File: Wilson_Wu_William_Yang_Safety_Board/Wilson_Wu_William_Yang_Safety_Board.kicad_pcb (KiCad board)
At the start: 2 copper layers, 122.4 x 171.4 mm, 115 parts, among them J1 22035035, J18 XT60-M, J2 22035035, J3 430450200, J4 M22-7130442, J5 430450200, J6 XT60-M, J7 XT60-M, J8 430450200, J9 Molex Micro-Fit 4 Pin, Q1 IRLML6344TRPBF, Q2 IRLML6344TRPBF, Q3 NTBLS0D8N08XTXG, Q4 NTBLS0D8N08XTXG, U1 STM32, U10 LTC4364HS, U11 LMV331IDBVR, U12 J115F11AH12VDCS61.5U, U13 ISOM8110DFGRQ1, U15 INA826AID, U16 J115F11AH12VDCS61.5U, U2 MCP2562-E_P, U3 10kohm, U4 SN74HCS21QPWRQ1, U5 J115F11AH12VDCS61.5U, U6 J115F11AH12VDCS61.5U, U7 LM1117IDTX-5.0/NOPB, U8 LM1117IMPX-ADJ/NOPB, U9 100 ohm

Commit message: layout
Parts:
- moved R106 12.0 mm to (95.2, 31.5)
- moved Q4 7.01 mm to (98.2, 38.7)
- moved C17 5.17 mm to (100.6, 21.1)
- moved U10 5.17 mm to (102.2, 25.8)
- moved C104 3.00 mm to (90.0, 32.4)
- moved R107 3.00 mm to (90.0, 30.8)
- moved R108 3.00 mm to (86.9, 30.8)
- moved R109 3.00 mm to (86.9, 32.4)
- moved Q3 0.35 mm to (103.7, 50.3)
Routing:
- net Net-(U10-DGATE): track 0.07 -> 18.8 mm
- net Net-(U10-~{SHDN}): track 11.8 -> 18.0 mm
- net Net-(U10-UV): track 20.9 -> 26.2 mm
- net Net-(D4-K): track 20.3 -> 25.7 mm
- net Net-(U10-OV): track 29.4 -> 34.7 mm

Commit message: holy
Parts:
- moved TP27 17.6 mm to (127.7, 16.6)
- moved C12 17.6 mm to (137.9, 17.5)
- moved J8 17.6 mm to (132.7, 16.6)
- moved TP10 6.66 mm to (103.5, 95.5)
- moved C1 4.78 mm to (132.2, 42.1)
- moved C2 4.78 mm to (140.9, 34.3)
- moved TP17 4.78 mm to (144.1, 34.3)
- moved U7 4.78 mm to (139.7, 38.9)
- moved H1 1.70 mm to (30.0, 163.8)
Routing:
- net Hydrogen-Output: track 116.8 -> 60.2 mm, vias 4 -> 2
- net load switch conn: track 4.82 -> 55.2 mm, vias 0 -> 2
- net Net-(U10-FB): track 1.77 -> 30.8 mm
- net +12V: track 249.9 -> 265.1 mm
- net /PA3: track 32.4 -> 35.5 mm
- net ignition signal: track 54.1 -> 52.0 mm
- net +5V: track 219.9 -> 217.9 mm
- net GND: track 54.1 -> 55.4 mm
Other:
- board size 122.4 x 171.4 mm -> 122.4 x 168.1 mm

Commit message: pcb layout
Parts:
- moved C103 1.19 mm to (108.4, 40.2)
- moved R105 1.19 mm to (108.4, 42.0)
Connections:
- C103 pad 2: Net-(U10-DGATE) -> Net-(U10-HGATE)
- R105 pad 1: Net-(U10-DGATE) -> Net-(U10-HGATE)
- R106 pad 3: (no net) -> load conn
- U10 pad 6: Net-(U10-DGATE) -> Net-(U10-HGATE)
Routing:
- net Net-(U10-HGATE): track 0.00 -> 15.2 mm
- net Net-(U10-DGATE): track 18.8 -> 18.1 mm, vias 0 -> 2
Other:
- board text added: "LTC4364HS"
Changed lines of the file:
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@@
 	(net 126 "Net-(U4-2D)")
 	(net 127 "Net-(U4-2C)")
+	(net 128 "Net-(U10-HGATE)")
 	(footprint "Diode_SMD:D_SOD-523"
 		(layer "F.Cu")
@@
 	(footprint "SMV_Passives:0603_resistors"
 		(layer "F.Cu")
-		(at 107.227799 42.25)
+		(at 108.377799 41.95)
 		(property "Reference" "R105"
 			(at -0.26 -1.1 0)
@@
 			(size 1.04 1.02)
 			(layers "F.Cu" "F.Mask" "F.Paste")
-			(net 39 "Net-(U10-DGATE)")
+			(net 128 "Net-(U10-HGATE)")
 			(pintype "passive")
 			(solder_mask_margin 0.102)
@@
 	(footprint "SMV_Passives:CAPC17595_87N_KEM"
 		(layer "F.Cu")
-		(at 107.25 40.5 180)
+		(at 108.4 40.2 180)
 		(tags "C0603C472K4RACTU ")
 		(property "Reference" "C103"
@@
 			(size 1.005599 0.949998)
 			(layers "F.Cu" "F.Mask" "F.Paste")
-			(net 39 "Net-(U10-DGATE)")
+			(net 128 "Net-(U10-HGATE)")
 			(pintype "passive")
 		)
@@
 			(polygon
 				(pts
-					(xy 107.4242 40.924199) (xy 107.0758 40.924199) (xy 107.0758 40.075801) (xy 107.4242 40.075801)
+					(xy 108.5742 40.624199) (xy 108.2258 40.624199) (xy 108.2258 39.775801) (xy 108.5742 39.775801)
 				)
 			)
@@
 			(layers "F.Cu" "F.Mask" "F.Paste")
 			(roundrect_rratio 0.25)
-			(net 39 "Net-(U10-DGATE)")
+			(net 128 "Net-(U10-HGATE)")
 			(pinfunction "HGATE")
 			(pintype "output")
@@
 			(pintype "passive")
 		)
-		(pad "2" smd rect
+		(pad "3" smd rect
 			(at 2.03 0 180)
 			(size 1.65 1.14)
 			(layers "F.Cu" "F.Mask" "F.Paste")
 			(net 58 "load conn")
-			(pintype "passive")
-		)
-		(pad "3" smd rect
-			(at -1.02 0 180)
-			(size 0.53 1.14)
-			(layers "F.Cu" "F.Mask" "F.Paste")
-		)
-		(pad "4" smd rect
-			(at 1.02 0 180)
-			(size 0.53 1.14)
-			(layers "F.Cu" "F.Mask" "F.Paste")
 		)
 		(embedded_fonts no)
@@
 	(gr_poly
 		(pts
-			(xy 108.5612 45.25) (xy 108.5612 41.8) (xy 107.5 41.8) (xy 107.5 45.25)
-		)
-		(stroke
-			(width 0.2)
-			(type solid)
-		)
-		(fill yes)
-		(layer "F.Cu")
-		(net 77)
-	)
-	(gr_poly
-		(pts
-			(xy 105.765402 39.771001) (xy 106.95 39.771001) (xy 106.95 43) (xy 106.629938 43.362941) (xy 103.35 43.3)
-			(xy 103.35 42.5) (xy 105.5 42.5) (xy 105.765402 42.234598)
-		)
-		(stroke
-			(width 0.2)
-			(type solid)
-		)
-		(fill yes)
-		(layer "F.Cu")
-		(net 39)
-	)
-	(gr_poly
-		(pts
 			(xy 132.75 45.3) (xy 132.75 55) (xy 121.25 66.5) (xy 121.25 77) (xy 111 77) (xy 111 69.5) (xy 116.25 64.25)
 			(xy 116.25 54) (xy 124.95 45.3)
@@
 	(gr_poly
 		(pts
-			(xy 99.6 26.996937) (xy 99.6 43.452338) (xy 99.6 43.452338) (xy 91.6588 43.452338) (xy 91.6588 33.541538)
-			(xy 91.703401 33.496937) (xy 95.05 33.6) (xy 96.8499 32.719653) (xy 96.855705 31.003439) (xy 98.5625 31)
-			(xy 98.6 29.784437) (xy 98.6 26.996937)
+			(xy 99.6 26.996937) (xy 99.6 43.452338) (xy 91.6588 43.452338) (xy 91.6588 33.541538) (xy 91.703401 33.496937)
+			(xy 95.05 33.6) (xy 96.8499 32.719653) (xy 96.855705 31.003439) (xy 98.5625 31) (xy 98.6 29.784437)
+			(xy 98.6 26.996937)
 		)
 		(stroke
@@
 	(gr_poly
 		(pts
-			(xy 102.25 27.2) (xy 103.3 27.2) (xy 103.5 27.2) (xy 103.5 33.544601) (xy 102.25 33.544601)
+			(xy 107.5 44.1) (xy 107.5 45.2) (xy 108.3 45.2) (xy 109.8 43.7) (xy 109.8 41.3) (xy 109.7 41.2) (xy 108.6 41.2)
+			(xy 108.6 43)
+		)
+		(stroke
+			(width 0.2)
+			(type solid)
+		)
+		(fill yes)
+		(layer "F.Cu")
+		(net 77)
+	)
+	(gr_poly
+		(pts
+			(xy 102.55 27.2) (xy 103.3 27.2) (xy 103.5 27.2) (xy 103.5 33.544601) (xy 102.55 33.544601)
 		)
 		(stroke
@@
 		(pts
 			(xy 118.9 38.3) (xy 118.8 38.299999) (xy 118.8 36.3) (xy 120.2 34.9) (xy 124.5 34.9) (xy 126 36.4)
-			(xy 126 40) (xy 126 40) (xy 116.7 40) (xy 116.5 39.8) (xy 116.5 38.4) (xy 116.7 38.3)
+			(xy 126 40) (xy 116.7 40) (xy 116.5 39.8) (xy 116.5 38.4) (xy 116.7 38.3)
 		)
 		(stroke
@@
 		(layer "Edge.Cuts")
 	)
+	(gr_text "LTC4364HS"
+		(at 111.5 1.3 0)
+		(layer "F.Cu")
+		(effects
+			(font
+				(size 1.27 1.27)
+			)
+		)
+	)
 	(segment
 		(start 96.85 81.8)
@@
 	)
 	(segment
-		(start 108.75 40.5)
-		(end 109.25 41)
-		(width 0.5)
-		(layer "F.Cu")
-		(net 2)
-	)
-	(segment
 		(start 77.65 124.425)
 		(end 77.65 125.6)
@@
 	)
 	(segment
+		(start 109.127799 38.927799)
+		(end 109.1 38.9)
+		(width 0.85)
+		(layer "F.Cu")
+		(net 2)
+	)
+	(segment
 		(start 118.2 32.2)
 		(end 117.8 31.8)
@@
 	)
 	(segment
-		(start 107.977799 40.5)
-		(end 108.75 40.5)
-		(width 0.5)
+		(start 109.127799 40.2)
+		(end 109.127799 38.927799)
+		(width 0.85)
 		(layer "F.Cu")
 		(net 2)
@@
 	)
 	(via
+		(at 109.1 38.9)
+		(size 0.6)
+		(drill 0.3)
+		(layers "F.Cu" "B.Cu")
+		(net 2)
+	)
+	(via
 		(at 54.75 124.4)
 		(size 0.6)
@@
 	)
 	(via
-		(at 109.25 41)
-		(size 0.6)
-		(drill 0.3)
-		(layers "F.Cu" "B.Cu")
-		(net 2)
-	)
-	(via
 		(at 116.5 31.8)
 		(size 0.6)
@@
 	)
 	(segment
-		(start 104.155 26.965468)
-		(end 104.155 28.225)
-		(width 0.5)
+		(start 101.615 29.885)
+		(end 101.6 29.9)
+		(width 0.85)
 		(layer "F.Cu")
 		(net 39)
 	)
 	(segment
-		(start 104.155 32.414568)
-		(end 106.522201 34.781769)
-		(width 0.5)
+		(start 105.6 42.8)
+		(end 103.8 42.8)
+		(width 0.85)
 		(layer "F.Cu")
 		(net 39)
 	)
 	(segment
-		(start 106.522201 34.781769)
-		(end 106.522201 40.5)
-		(width 0.5)
+		(start 101.615 28.225)
+		(end 101.615 29.885)
+		(width 0.85)
 		(layer "F.Cu")
 		(net 39)
 	)
 	(segment
-		(start 104.155 28.225)
-		(end 104.155 32.414568)
-		(width 0.5)
+		(start 103.8 42.8)
+		(end 103.75 42.85)
+		(width 0.85)
 		(layer "F.Cu")
 		(net 39)
 	)
-	(segment
-		(start 101.615 26.855768)
-		(end 102.021768 26.449)
-		(width 0.5)
-		(layer "F.Cu")
+	(via
+		(at 105.6 42.8)
+		(size 0.6)
+		(drill 0.3)
+		(layers "F.Cu" "B.Cu")
 		(net 39)
 	)
-	(segment
-		(start 103.638532 26.449)
-		(end 104.155 26.965468)
-		(width 0.5)
-		(layer "F.Cu")
+	(via
+		(at 101.6 29.9)
+		(size 0.6)
+		(drill 0.3)
+		(layers "F.Cu" "B.Cu")
 		(net 39)
 	)
 	(segment
-		(start 101.615 28.225)
-		(end 101.615 26.855768)
-		(width 0.5)
-		(layer "F.Cu")
+		(start 101.6 29.9)
+		(end 101.6 38.8)
+		(width 6.75)
+		(layer "B.Cu")
 		(net 39)
 	)
 	(segment
-		(start 102.021768 26.449)
-		(end 103.638532 26.449)
-		(width 0.5)
-		(layer "F.Cu")
+		(start 101.6 38.8)
+		(end 105.6 42.8)
+		(width 6.75)
+		(layer "B.Cu")
 		(net 39)
 	)
@@
 	(segment
 		(start 112.630024 44.130024)
-		(end 112.630024 42.430024)
+		(end 114.000001 45.500001)
 		(width 0.75)
 		(layer "F.Cu")
@@
 	)
 	(segment
-		(start 109.1743 35.4257)
-		(end 106.695 32.9464)
-		(width 0.85)
-		(layer "F.Cu")
-		(net 107)
-	)
-	(segment
-		(start 114.000001 45.500001)
-		(end 115.8498 45.500001)
+		(start 110.9 40.7)
+		(end 112.630024 42.430024)
 		(width 0.75)
 		(layer "F.Cu")
@@
 	)
 	(segment
-		(start 113.125 44.625)
+		(start 112.630024 42.430024)
 		(end 112.630024 44.130024)
 		(width 0.75)
@@
 	)
 	(segment
-		(start 112.630024 42.430024)
-		(end 109.1743 38.9743)
+		(start 111.2076 37.458999)
+		(end 111.849213 37.458999)
 		(width 0.75)
 		(layer "F.Cu")
@@
 	)
 	(segment
-		(start 113.125 44.625)
-		(end 114.000001 45.500001)
+		(start 110.9 37.1514)
+		(end 110.9 40.7)
 		(width 0.75)
 		(layer "F.Cu")
@@
 	)
 	(segment
-		(start 111.2076 37.458999)
-		(end 111.849213 37.458999)
-		(width 0.75)
+		(start 106.695 32.9464)
+		(end 106.695 28.225)
+		(width 0.85)
 		(layer "F.Cu")
 		(net 107)
 	)
 	(segment
-		(start 109.1743 38.9743)
-		(end 109.1743 35.4257)
+		(start 109.1743 35.4257)
+		(end 110.9 37.1514)
 		(width 0.75)
 		(layer "F.Cu")
@@
 	)
 	(segment
-		(start 106.695 32.9464)
-		(end 106.695 28.225)
+		(start 109.1743 35.4257)
+		(end 106.695 32.9464)
 		(width 0.85)
 		(layer "F.Cu")
@@
 	)
 	(segment
+		(start 114.000001 45.500001)
+		(end 115.8498 45.500001)
+		(width 0.75)
+		(layer "F.Cu")
+		(net 107)
+	)
+	(segment
 		(start 87.851 30.489)
 		(end 87.851 17.749)
@@
 		(net 127)
 	)
+	(segment
+		(start 107.672201 40.2)
+		(end 107.672201 41.920598)
+		(width 0.85)
+		(layer "F.Cu")
+		(net 128)
+	)
+	(segment
+		(start 105.644 38.171799)
+		(end 107.672201 40.2)
+		(width 0.85)
+		(layer "F.Cu")
+		(net 128)
+	)
+	(segment
+		(start 104.226 29.102586)
+		(end 104.226 28.225)
+		(width 0.85)
+		(layer "F.Cu")
+		(net 128)
+	)
+	(segment
+		(start 105.644 30.520586)
+		(end 104.226 29.102586)
+		(width 0.85)
+		(layer "F.Cu")
+		(net 128)
+	)
+	(segment
+		(start 107.672201 41.920598)
+		(end 107.642799 41.95)
+		(width 0.85)
+		(layer "F.Cu")
+		(net 128)
+	)
+	(segment
+		(start 105.644 30.520586)
+		(end 105.644 38.171799)
+		(width 0.85)
+		(layer "F.Cu")
+		(net 128)
+	)
 	(zone

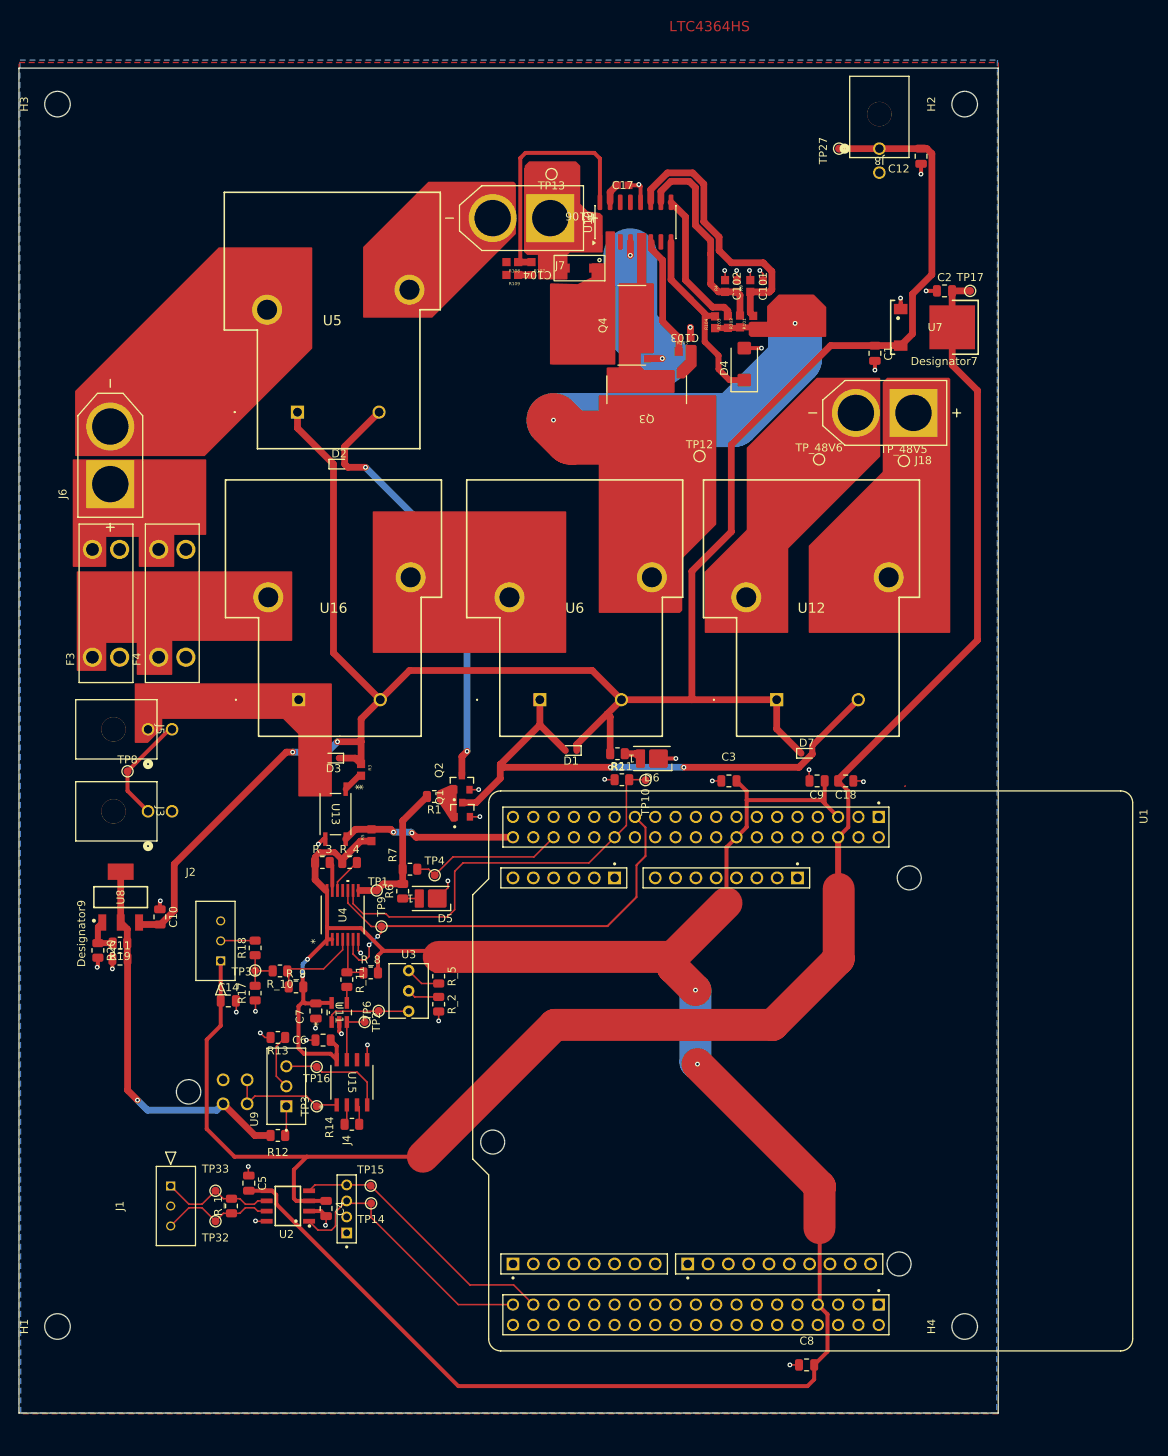
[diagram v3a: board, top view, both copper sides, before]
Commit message: Power thingy revamp + Silkscreen Updates
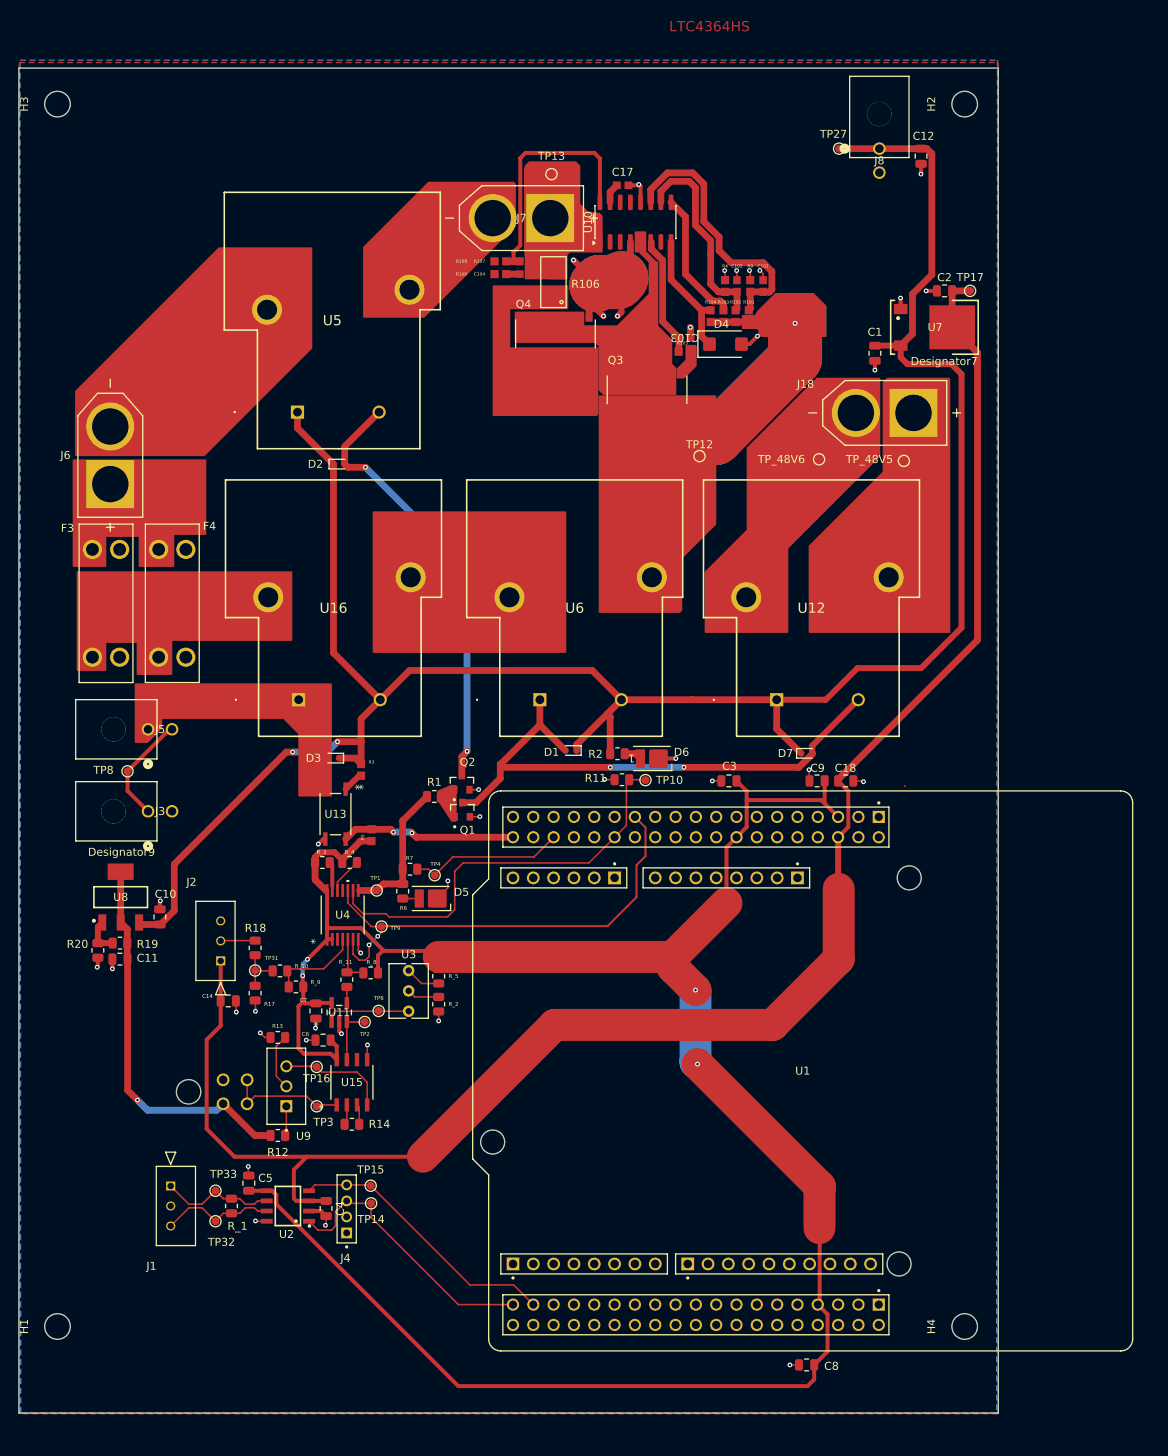
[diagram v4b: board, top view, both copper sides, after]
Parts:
- moved Q4 7.55 mm to (92.3, 43.3), turned to 180 degrees
- moved D4 6.26 mm to (111.5, 41.0), turned to 0 degrees
- moved R106 3.69 mm to (92.0, 33.2), turned to 90 degrees
- moved R108 1.50 mm to (85.4, 30.6)
- moved R109 1.50 mm to (85.4, 32.2)
- moved C104 1.50 mm to (88.5, 32.2)
- moved R107 1.50 mm to (88.5, 30.6)
- moved R104 0.94 mm to (111.7, 37.5)
- moved R103 0.92 mm to (113.2, 37.5)
- moved R101 0.89 mm to (116.4, 37.5)
- moved R102 0.87 mm to (114.8, 37.5)
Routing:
- net Net-(U10-DGATE): track 18.1 -> 30.0 mm, vias 2 -> 3
- net +12V: track 265.1 -> 276.5 mm
- net Net-(D4-K): track 25.7 -> 15.9 mm
- net load switch conn: track 55.2 -> 59.0 mm, vias 2 -> 1
- net Net-(U10-~{SHDN}): track 18.0 -> 16.8 mm
- net Net-(U10-OV): track 34.7 -> 33.9 mm
- net Net-(U10-UV): track 26.2 -> 25.4 mm
